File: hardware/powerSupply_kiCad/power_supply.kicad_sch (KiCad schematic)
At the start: 5 parts

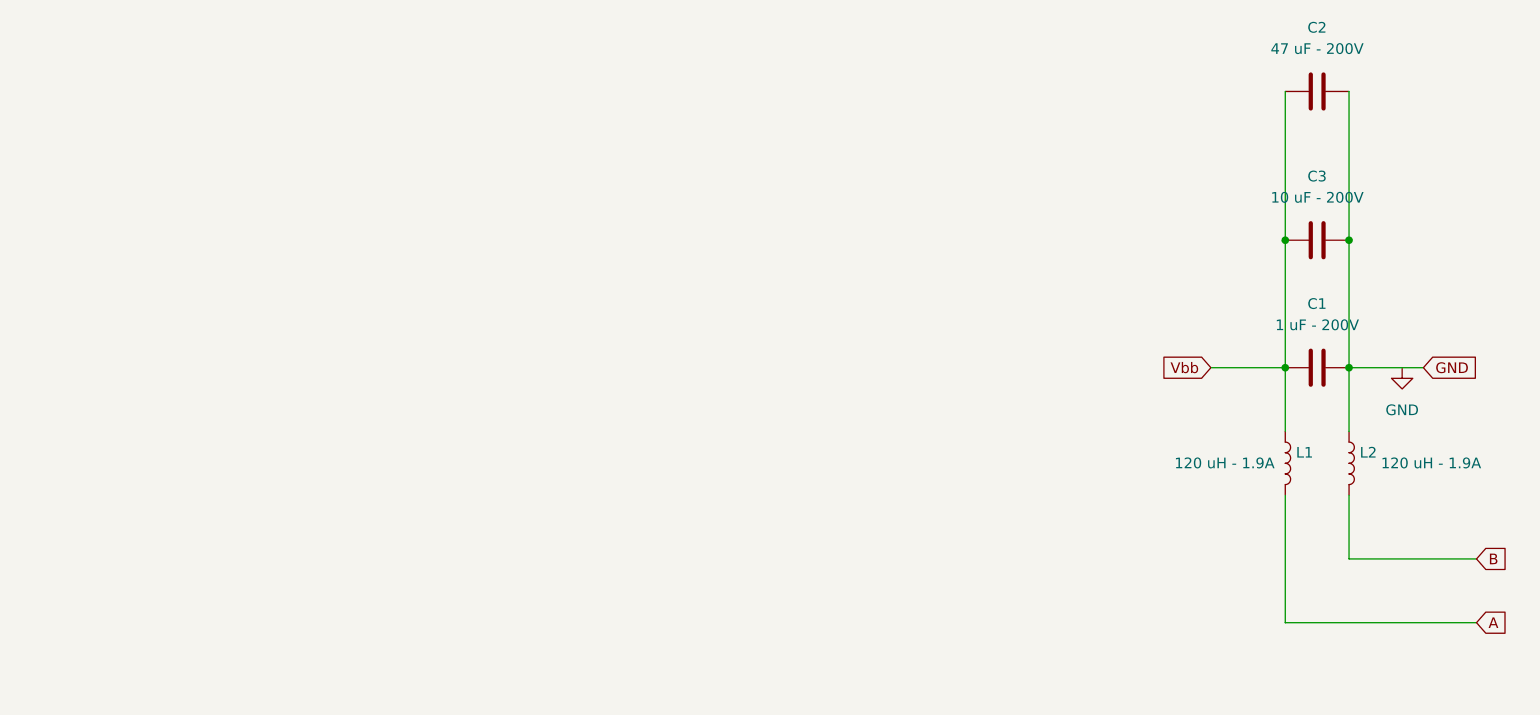
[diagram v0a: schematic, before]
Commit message: added the LT7101 to the power supply sch
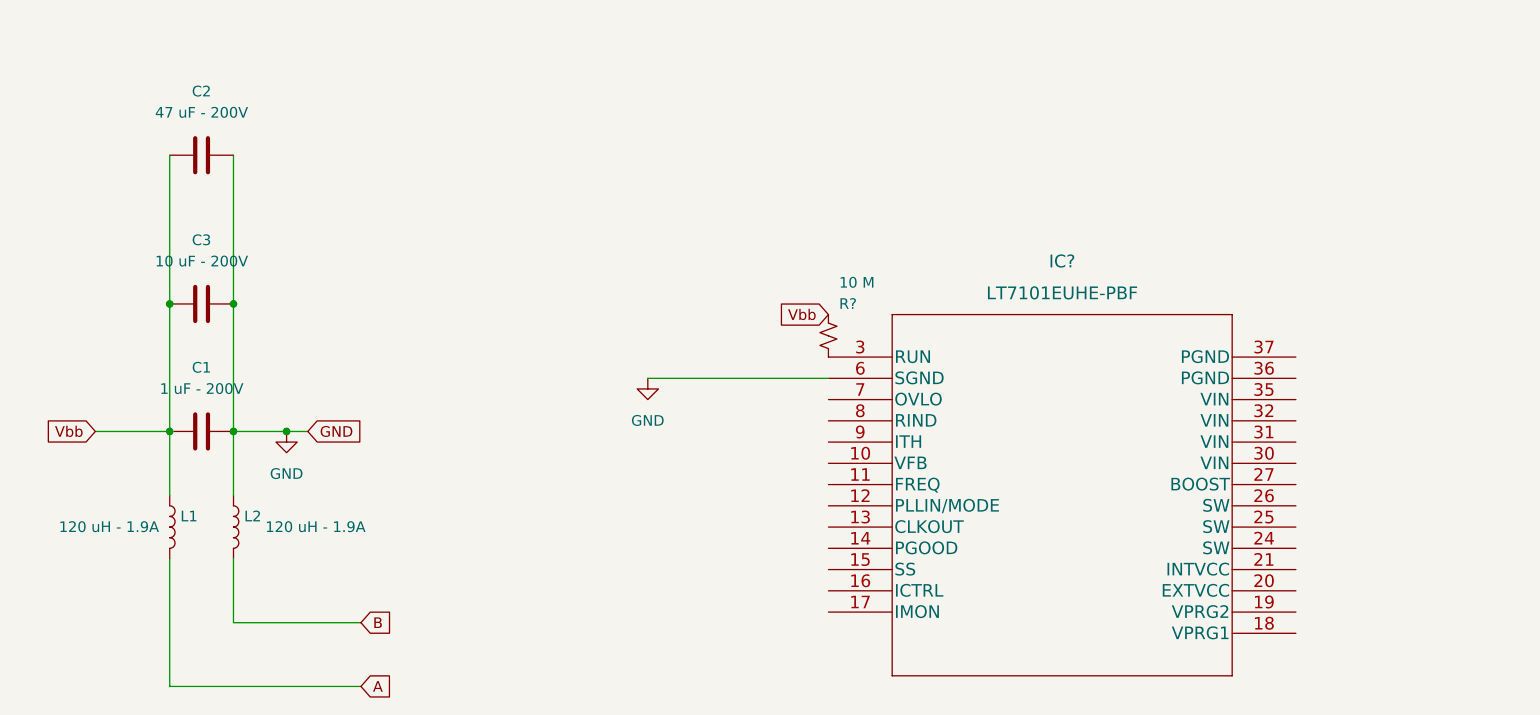
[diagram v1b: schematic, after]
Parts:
- added IC?: LT7101EUHE-PBF, bib:LT7101EUHE-PBF, symbol LT7101:LT7101EUHE-PBF
- added R?: 10 M, symbol Device:R_Small_US
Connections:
- net GND: now also IC?.6 (SGND)
- net Vbb: now also R?.1
- new net: IC?.3 (RUN), R?.2
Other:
- moved on the sheet: C1, C2, C3, L1, L2

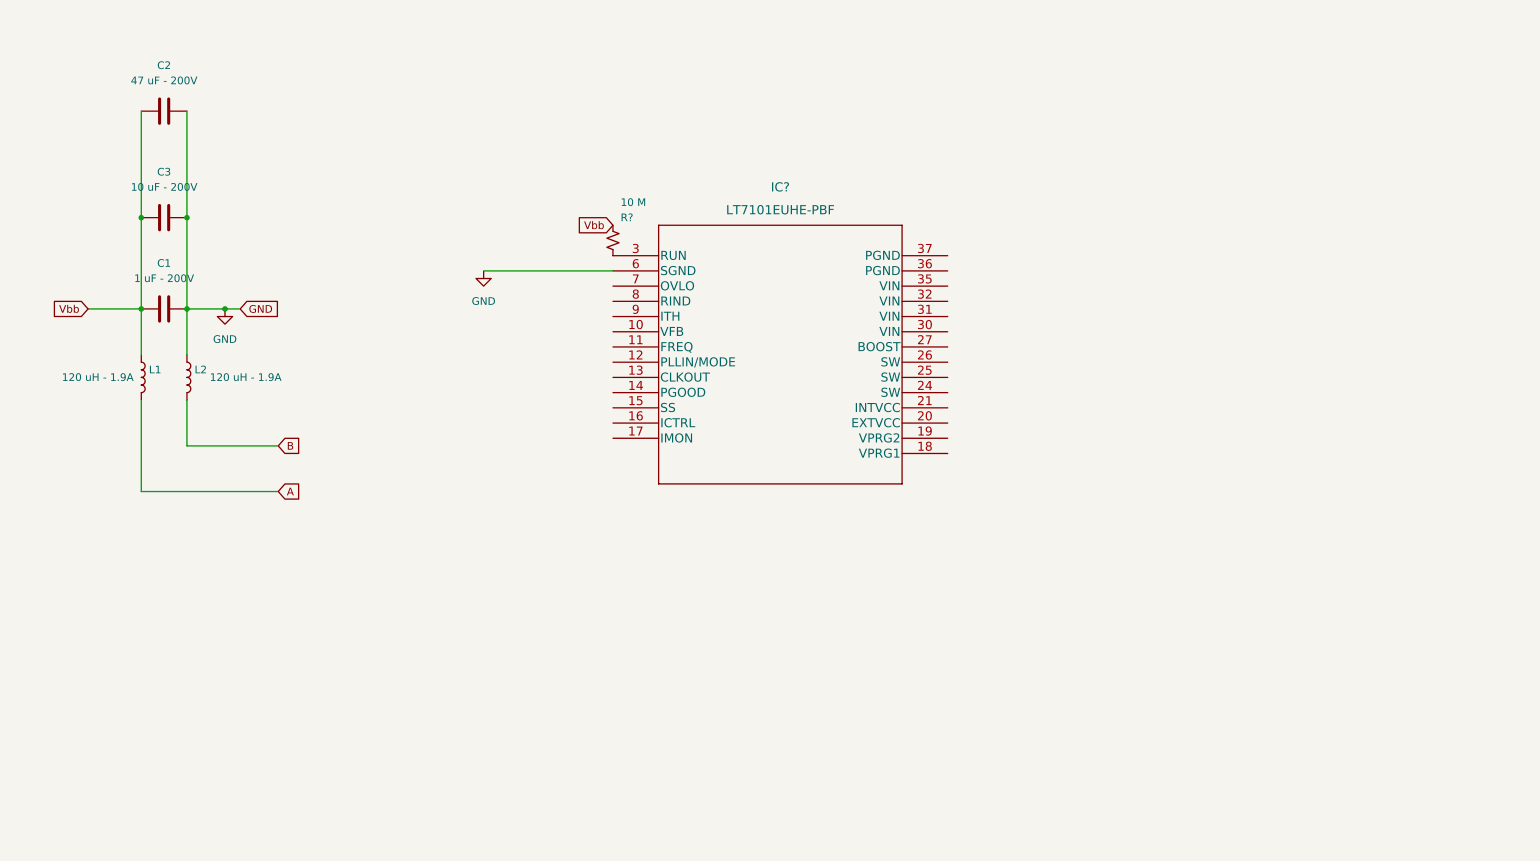
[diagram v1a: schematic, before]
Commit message: Added components around the  LT7101 SMPS
Copying the component selection of the DC2895A1 demo board. No footprints are selected for now, only symbols
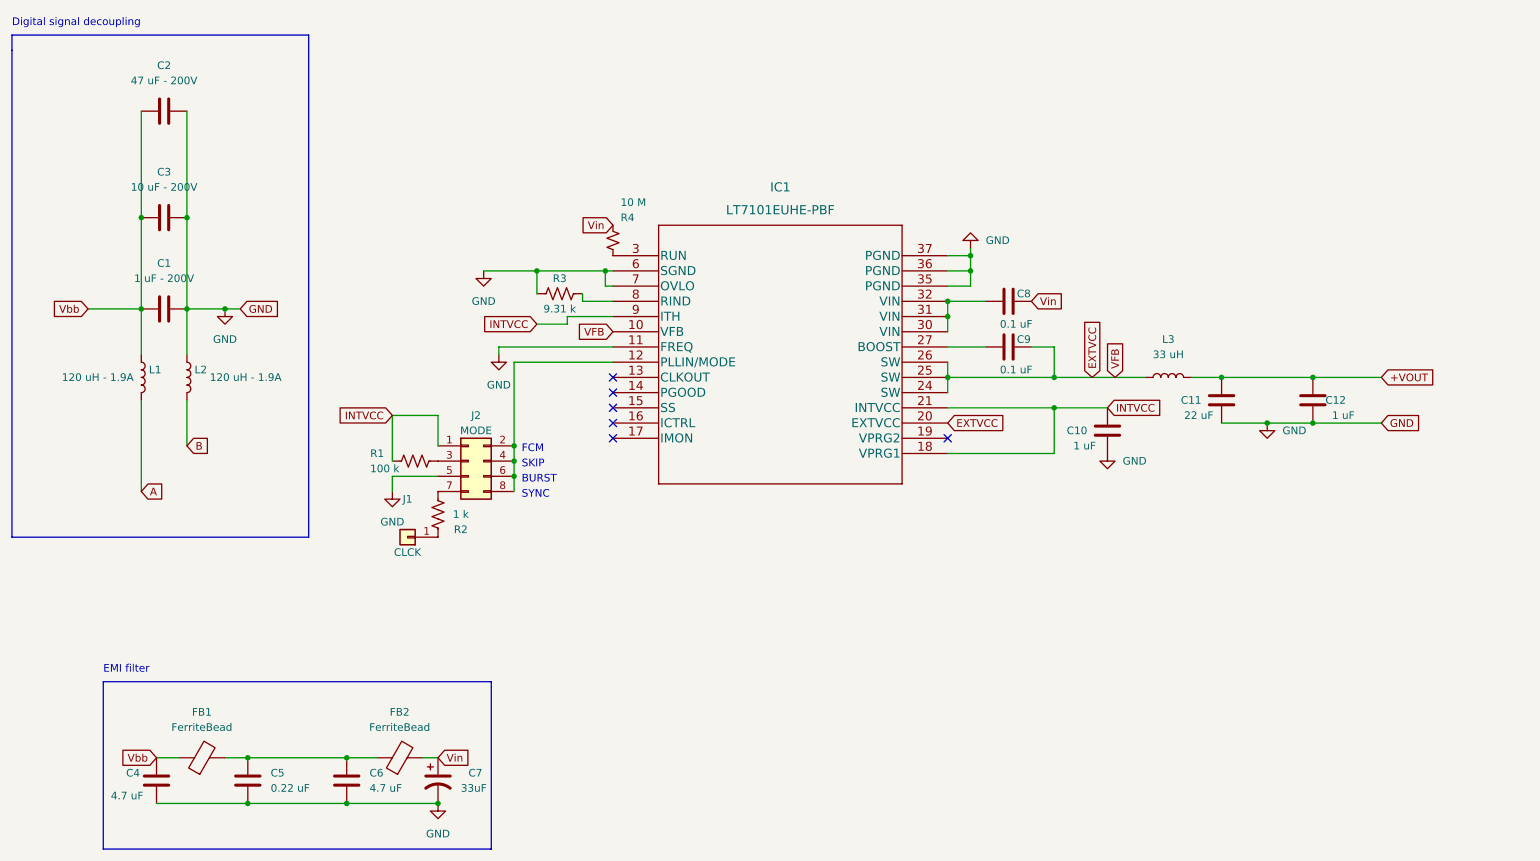
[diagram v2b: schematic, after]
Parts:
- added C10, C12: 1 uF, symbol Device:C
- added C11: 22 uF, symbol Device:C
- added C4, C6: 4.7 uF, symbol Device:C
- added C5: 0.22 uF, symbol Device:C
- added C7: 33uF, symbol Device:C_Polarized_US
- added C8, C9: 0.1 uF, symbol Device:C
- added FB1, FB2: FerriteBead, symbol Device:FerriteBead
- added J1: CLCK, symbol Connector_Generic:Conn_01x01
- added J2: MODE, symbol Connector_Generic:Conn_02x04_Odd_Even
- added L3: 33 uH, symbol Device:L
- added R1: 100 k, symbol Device:R_US
- added R2: 1 k, symbol Device:R_US
- added R3: 9.31 k, symbol Device:R_US
- gave numbers to parts that had none: 2
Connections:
- net GND: now also IC1.11 (FREQ), IC1.35 (PGND), IC1.36 (PGND), IC1.37 (PGND), IC1.7 (OVLO), C10.2, C11.2, C12.2, C4.2, C5.2, C6.2, C7.2, J2.5 (Pin_5), R3.1
- net Vbb: now also C4.1, FB1.1; no longer R4.1
- net EXTVCC: now reaches IC1.10 (VFB)
- net EXTVCC: now also IC1.20 (EXTVCC), IC1.24 (SW), IC1.25 (SW), IC1.26 (SW), C9.2, L3.1
- net at IC1.12 (PLLIN/MODE): now also J2.2 (Pin_2), J2.4 (Pin_4), J2.6 (Pin_6), J2.8 (Pin_8)
- net INTVCC: now reaches IC1.18 (VPRG1)
- net INTVCC: now also IC1.21 (INTVCC), IC1.9 (ITH), C10.1, J2.1 (Pin_1), R1.1
- net at IC1.27 (BOOST): now also C9.1
- net at IC1.30 (VIN): now also IC1.31 (VIN), IC1.32 (VIN), C8.1
- net at IC1.8 (RIND): now also R3.2
- new net: J2.3 (Pin_3), R1.2
- new net: J2.7 (Pin_7), R2.2
- new net: J1.1 (Pin_1), R2.1
- new net: C5.1, C6.1, FB1.2, FB2.1
- new net +VOUT: C11.1, C12.1, L3.2
- new net Vin: C7.1, C8.2, FB2.2, R4.1
- no-connect marks 0 -> 6
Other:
- note added: "BURST"
- note added: "Digital signal decoupling"
- note added: "EMI filter"
- note added: "FCM"
- note added: "SKIP"
- note added: "SYNC"

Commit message: symbol to footprint association for power supply
Datasheet and footprint added to every component. all component are stored in the digikey cart
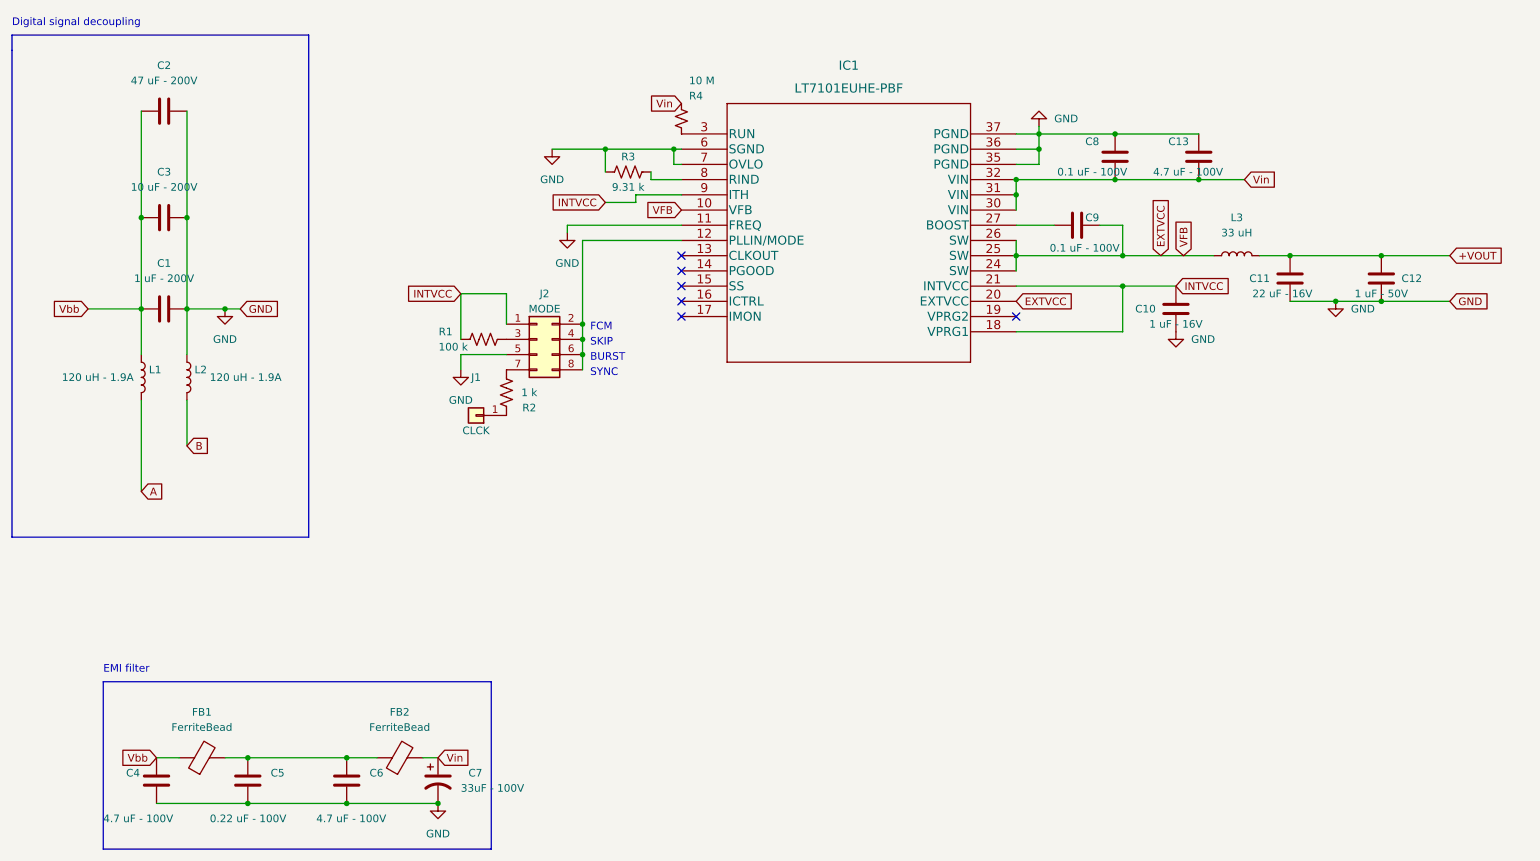
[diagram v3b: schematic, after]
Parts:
- added C13: 4.7 uF - 100V, Capacitor_SMD:C_1210_3225Metric, symbol Device:C
- C10: value 1 uF -> 1 uF - 16V; footprint (none) -> Capacitor_SMD:C_0805_2012Metric
- C11: value 22 uF -> 22 uF - 16V; footprint (none) -> Capacitor_SMD:C_1210_3225Metric
- C12: value 1 uF -> 1 uF - 50V; footprint (none) -> Capacitor_SMD:C_0805_2012Metric
- C4, C6: value 4.7 uF -> 4.7 uF - 100V; footprint (none) -> Capacitor_SMD:C_1210_3225Metric
- C5: value 0.22 uF -> 0.22 uF - 100V; footprint (none) -> Capacitor_SMD:C_0805_2012Metric
- C7: value 33uF -> 33uF - 100V; footprint (none) -> Capacitor_SMD:CP_Elec_10x10.5
- C8, C9: value 0.1 uF -> 0.1 uF - 100V; footprint (none) -> Capacitor_SMD:C_0805_2012Metric
- FB1, FB2: footprint (none) -> Capacitor_SMD:C_0805_2012Metric
- J1: footprint (none) -> Connector_PinHeader_2.54mm:PinHeader_1x01_P2.54mm_Vertical
- J2: footprint (none) -> Connector_PinHeader_2.54mm:PinHeader_2x04_P2.54mm_Vertical
- L3: footprint (none) -> bib:SPM7054VT
- R1, R2, R3: footprint (none) -> Resistor_SMD:R_0603_1608Metric
- R4: footprint (none) -> Resistor_SMD:R_0805_2012Metric
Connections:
- net GND: now also C8.2, C13.1
- net Vin: now also C8.1, IC1.30 (VIN), IC1.31 (VIN), IC1.32 (VIN), C13.2; no longer C8.2
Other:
- moved on the sheet: C10, C11, C12, C8, C9, IC1, J1, J2, L3, R1, R2, R3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

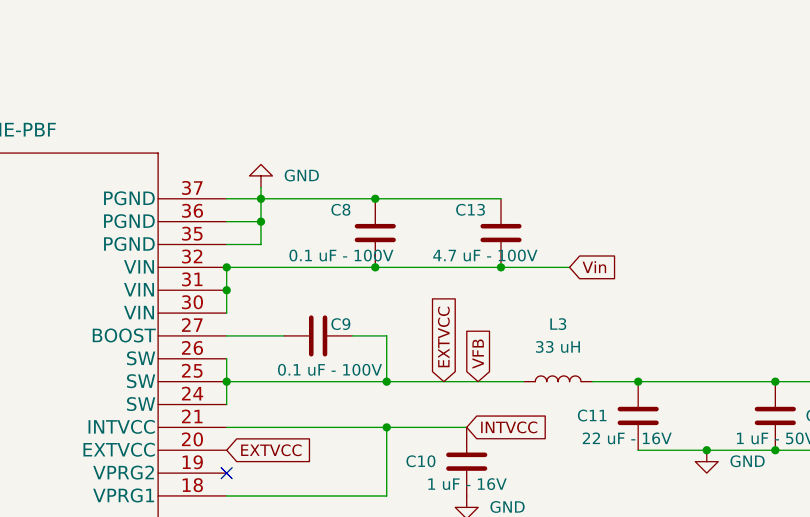
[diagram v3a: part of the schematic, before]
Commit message: Preliminary placement of components on the power supply board
3 planes are : Vbb or Vin, GND (top and bottom) and Vout
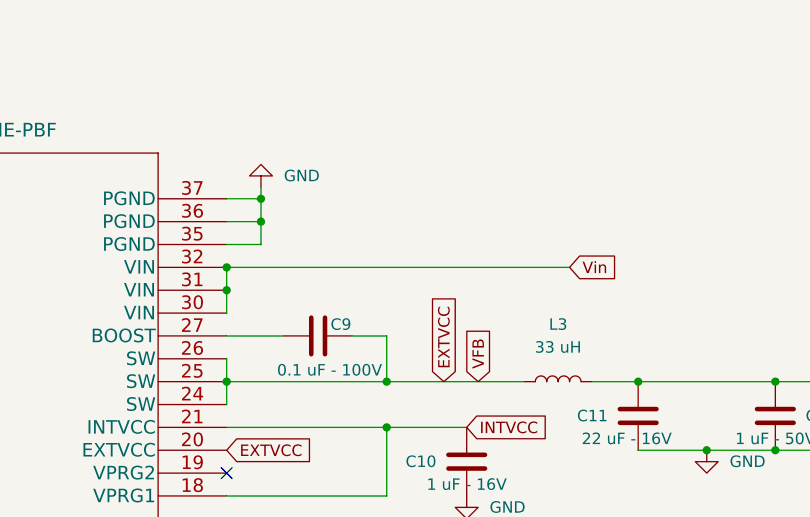
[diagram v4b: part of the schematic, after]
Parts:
- removed C13: 4.7 uF - 100V, Capacitor_SMD:C_1210_3225Metric, symbol Device:C
- removed C8: 0.1 uF - 100V, Capacitor_SMD:C_0805_2012Metric, symbol Device:C
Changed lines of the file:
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@@
 (kicad_sch (version 20211123) (generator eeschema)
   (paper "A4")
-  (junction (at 213.36 58.42) (diameter 0) (color 0 0 0 0)
-  )
   (junction (at 257.81 71.12) (diameter 0) (color 0 0 0 0)
   )
@@
   (junction (at 257.81 78.74) (diameter 0) (color 0 0 0 0)
   )
-  (junction (at 213.36 50.8) (diameter 0) (color 0 0 0 0)
-  )
   (junction (at 58.42 64.77) (diameter 0) (color 0 0 0 0)
   )
@@
   )
   (junction (at 128.27 53.34) (diameter 0) (color 0 0 0 0)
-  )
-  (junction (at 227.33 58.42) (diameter 0) (color 0 0 0 0)
   )
   (junction (at 100.33 162.56) (diameter 0) (color 0 0 0 0)
@@
     (stroke (width 0) (type default) (color 0 0 0 0))
   )
-  (wire (pts (xy 196.85 58.42) (xy 213.36 58.42))
-    (stroke (width 0) (type default) (color 0 0 0 0))
-  )
   (wire (pts (xy 119.38 53.34) (xy 128.27 53.34))
     (stroke (width 0) (type default) (color 0 0 0 0))
@@
     (stroke (width 0) (type default) (color 0 0 0 0))
   )
-  (wire (pts (xy 213.36 50.8) (xy 227.33 50.8))
-    (stroke (width 0) (type default) (color 0 0 0 0))
-  )
   (wire (pts (xy 58.42 46.99) (xy 58.42 64.77))
     (stroke (width 0) (type default) (color 0 0 0 0))
@@
     (stroke (width 0) (type default) (color 0 0 0 0))
   )
-  (wire (pts (xy 227.33 58.42) (xy 234.95 58.42))
-    (stroke (width 0) (type default) (color 0 0 0 0))
-  )
   (wire (pts (xy 200.66 50.8) (xy 200.66 49.53))
     (stroke (width 0) (type default) (color 0 0 0 0))
@@
     (stroke (width 0) (type default) (color 0 0 0 0))
   )
-  (wire (pts (xy 200.66 50.8) (xy 213.36 50.8))
-    (stroke (width 0) (type default) (color 0 0 0 0))
-  )
   (wire (pts (xy 50.8 46.99) (xy 50.8 64.77))
     (stroke (width 0) (type default) (color 0 0 0 0))
@@
     (stroke (width 0) (type default) (color 0 0 0 0))
   )
-  (wire (pts (xy 213.36 58.42) (xy 227.33 58.42))
+  (wire (pts (xy 196.85 58.42) (xy 234.95 58.42))
     (stroke (width 0) (type default) (color 0 0 0 0))
   )
@@
     (pin "8")
   )
-  (symbol (lib_id "Device:C") (at 213.36 54.61 180) (unit 1)
-    (in_bom yes) (on_board yes)
-    (property "Reference" "C8" (id 0) (at 209.55 52.07 0))
-    (property "Value" "0.1 uF - 100V" (id 1) (at 209.55 57.15 0))
-    (property "Footprint" "Capacitor_SMD:C_0805_2012Metric" (id 2) (at 212.3948 50.8 0)
-      (effects (font (size 1.27 1.27)) hide)
-    )
-    (property "Datasheet" "https://www.digikey.ca/en/products/detail/murata-electronics/GRM21BR72A104KAC4L/4905550?s=N4IgTCBcDaIOICUCyYCMAhBB2MBBVADACwDSuAwkQDIgC6AvkA" (id 3) (at 213.36 54.61 0)
-      (effects (font (size 1.27 1.27)) hide)
-    )
-    (pin "1")
-    (pin "2")
-  )
   (symbol (lib_id "Device:C") (at 207.01 66.04 90) (unit 1)
     (in_bom yes) (on_board yes)
@@
     )
     (pin "1")
-  )
-  (symbol (lib_id "Device:C") (at 227.33 54.61 0) (unit 1)
-    (in_bom yes) (on_board yes)
-    (property "Reference" "C13" (id 0) (at 222.25 52.07 0)
-      (effects (font (size 1.27 1.27)) (justify left))
-    )
-    (property "Value" "4.7 uF - 100V" (id 1) (at 219.71 57.15 0)
-      (effects (font (size 1.27 1.27)) (justify left))
-    )
-    (property "Footprint" "Capacitor_SMD:C_1210_3225Metric" (id 2) (at 228.2952 58.42 0)
-      (effects (font (size 1.27 1.27)) hide)
-    )
-    (property "Datasheet" "https://www.digikey.ca/en/products/detail/taiyo-yuden/HMK325C7475KN-TE/6563631" (id 3) (at 227.33 54.61 0)
-      (effects (font (size 1.27 1.27)) hide)
-    )
-    (pin "1")
-    (pin "2")
   )
   (symbol (lib_id "power:GND") (at 250.19 78.74 0) (unit 1)
@@
       (reference "C7") (unit 1) (value "33uF - 100V") (footprint "Capacitor_SMD:CP_Elec_10x10.5")
     )
-    (path "/1d3033cd-a08e-4f55-a285-b7fa49134826"
-      (reference "C8") (unit 1) (value "0.1 uF - 100V") (footprint "Capacitor_SMD:C_0805_2012Metric")
-    )
     (path "/1ef07e4c-511c-49d7-a9f4-369aabbc22ed"
       (reference "C9") (unit 1) (value "0.1 uF - 100V") (footprint "Capacitor_SMD:C_0805_2012Metric")
@@
       (reference "C12") (unit 1) (value "1 uF - 50V") (footprint "Capacitor_SMD:C_0805_2012Metric")
     )
-    (path "/4dcd3bc6-fb1d-4700-ac76-d8b362c53bbe"
-      (reference "C13") (unit 1) (value "4.7 uF - 100V") (footprint "Capacitor_SMD:C_1210_3225Metric")
-    )
     (path "/748f3342-cf40-4469-960e-8d7c515a3ace"
